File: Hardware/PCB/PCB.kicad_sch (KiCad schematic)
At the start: 74 parts, among them CN1 XT30UPB-M, CN2 2060-453-HDGC, CN3 2060-452-HDGC, CN4 2060-453-HDGC, CN6 2060-453-HDGC, CN7 2060-453-HDGC, J1 Connector, USB-TYPE-C-16P, SW1 TS-1187A-B-A-B, U1 RP2350B_C42415655, U3 BMP581, U4 ICM-45686, U5 BQ25883RGER, U6 LMR51430YFDDCR, U7 TPS630701RNMR, U8 GD25Q128ESIGR, X2 X322512MSB4SI

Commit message: finishing up schem
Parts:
- removed CN2, CN4, CN6, CN7: 2060-453-HDGC, easyeda2kicad:CONN-SMD_2060-453-HDGC, symbol easyeda2kicad:2060-453-HDGC
- removed CN3: 2060-452-HDGC, easyeda2kicad:CONN-SMD_2060-452-HDGC, symbol easyeda2kicad:2060-452-HDGC
- added U10, U11, U12, U9: KF128-2.54-3P, easyeda2kicad:CONN-TH_3P-P2.54_KF128-2.54-3P, symbol easyeda2kicad:KF128-2.54-3P
- added U2: KF128-2.54-2P, easyeda2kicad:CONN-TH_P2.54_KF128-2.54-2P, symbol easyeda2kicad:KF128-2.54-2P
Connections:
- net +7.5V: now also U9.2
- net GND: now also U10.3, U11.3, U12.3, U2.1, U9.3
- net at C2.1, CN1.2 (+), U5.13 (BAT)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: now also U2.2
- net at C23.2, C24.1, C26.2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: now also U10.2, U11.2, U12.2
- net at U1.23 (GPIO23): now also U12.1
- net at U1.22 (GPIO22): now also U10.1
- net at U1.21 (GPIO21): now also U9.1
- net at U1.25 (GPIO24): now also U11.1

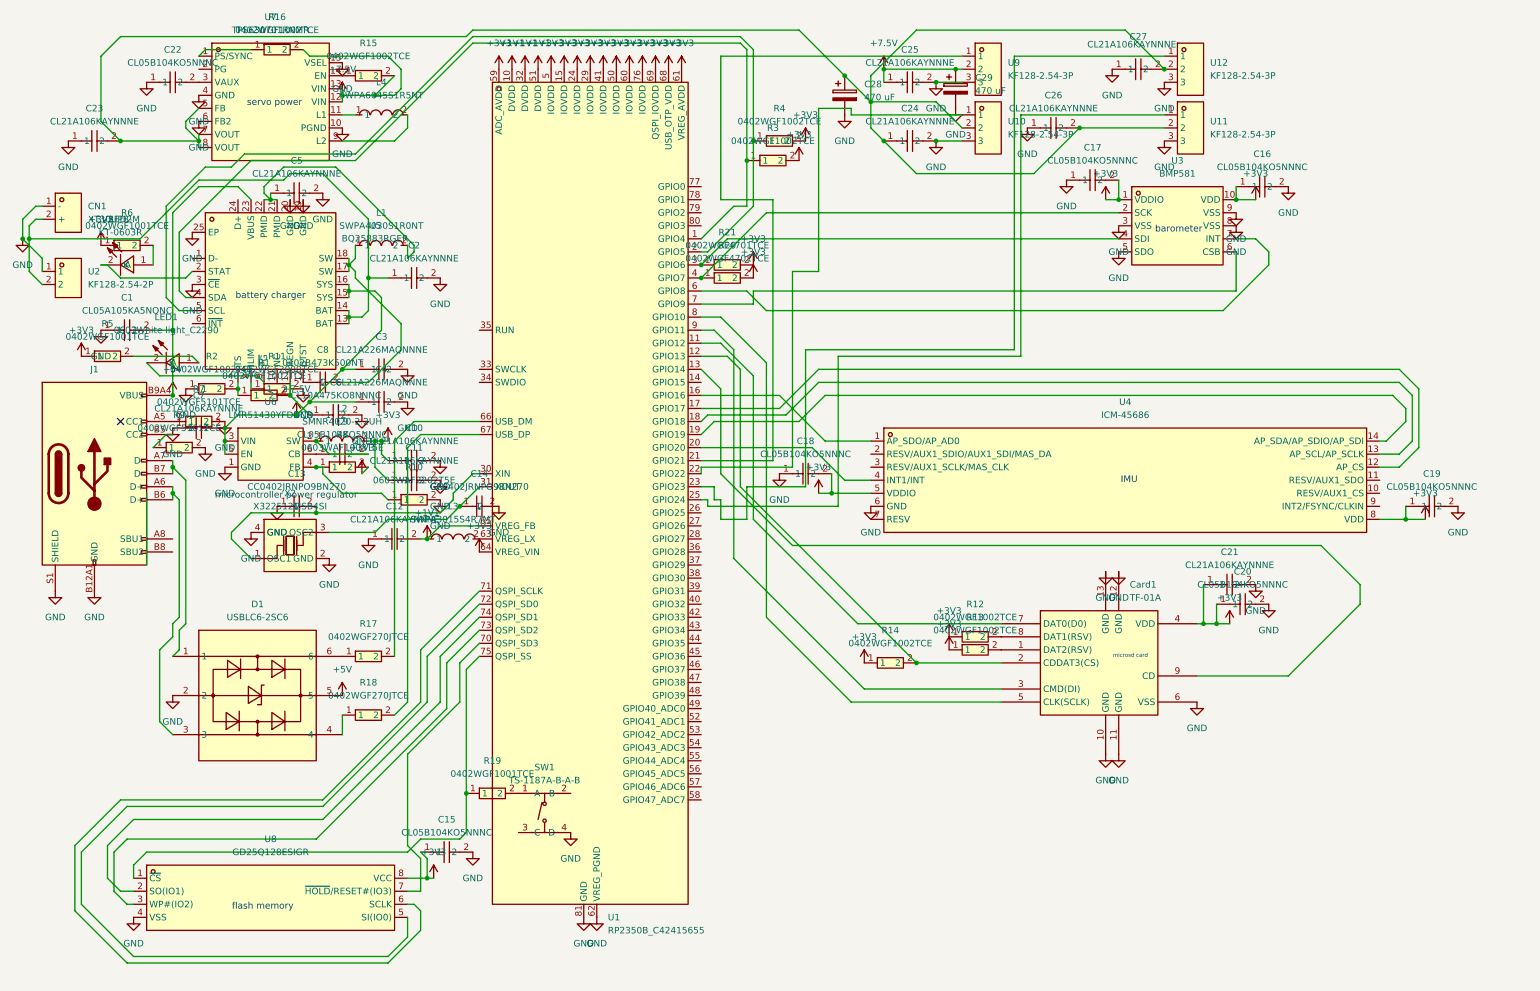
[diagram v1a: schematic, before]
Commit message: PCB routing started, added BOM.CSV
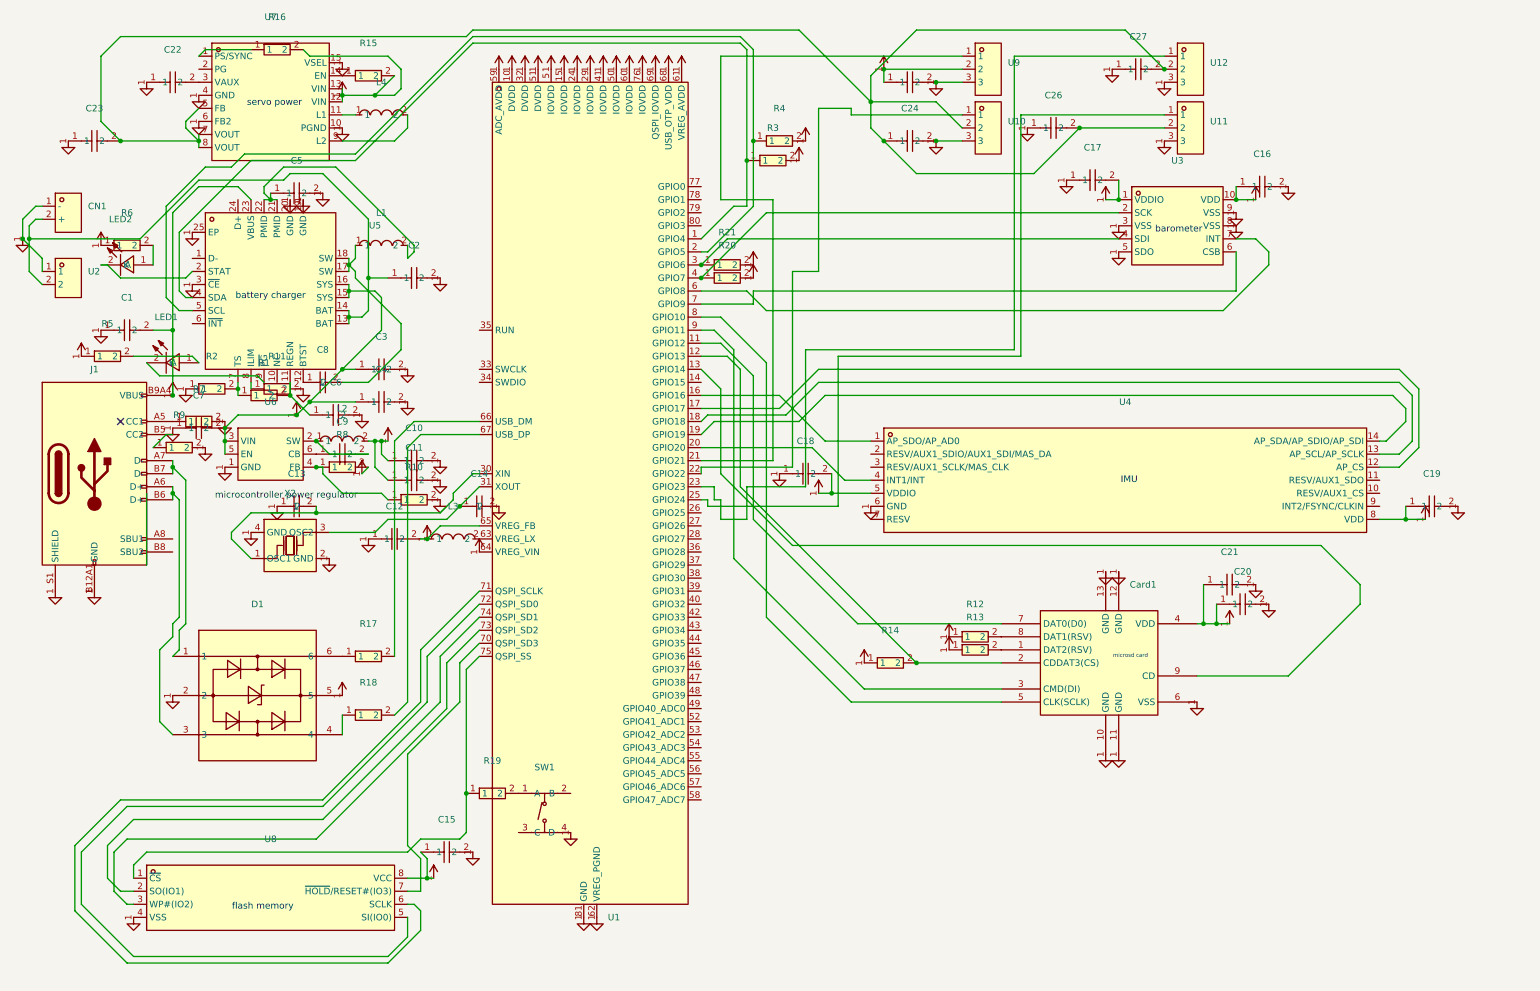
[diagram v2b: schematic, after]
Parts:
- removed C28, C29: 470 uF, Capacitor_SMD:CP_Elec_8x10.5, symbol Device:C_Polarized

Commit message: Battery charging added to PCB
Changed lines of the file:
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@@
 	)
 	(junction
+		(at 185.42 17.78)
+		(diameter 0)
+		(color 0 0 0 0)
+	)
+	(junction
 		(at 191.77 20.32)
 		(diameter 0)
@@
 		(at 33.02 86.36)
 	)
+	(bus_entry
+		(at 118.11 90.17)
+		(size 2.54 2.54)
+		(stroke
+			(width 0)
+			(type default)
+		)
+	)
 	(wire
 		(pts
@@
 	(wire
 		(pts
+			(xy 185.42 17.78) (xy 196.85 17.78)
+		)
+		(stroke
+			(width 0)
+			(type default)
+		)
+	)
+	(wire
+		(pts
 			(xy 71.12 90.17) (xy 73.66 92.71)
 		)
@@
 	(wire
 		(pts
-			(xy 181.61 17.78) (xy 196.85 17.78)
+			(xy 181.61 17.78) (xy 185.42 17.78)
 		)
 		(stroke
@@
 		)
 		(stroke
+			(width 0)
+			(type default)
+		)
+	)
+	(wire
+		(pts
+			(xy 185.42 19.05) (xy 185.42 17.78)
+		)
+		(stroke

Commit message: Restarting PCB, finished Flash memory application
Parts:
- added C28, C29, C30, C32, C33, C34, C35, C36, C37, C38, C39, C40: CL05B104KO5NNNC, easyeda2kicad:C0402, symbol easyeda2kicad:CL05B104KO5NNNC
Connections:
- net +1V1: now also C28.1, C29.1, C30.1
- net +3V3: now also C32.1, C33.1, C34.1, C35.1, C36.1, C37.1, C38.1, C39.1, C40.1
- net GND: now also C28.2, C29.2, C30.2, C32.2, C33.2, C34.2, C35.2, C36.2, C37.2, C38.2, C39.2, C40.2

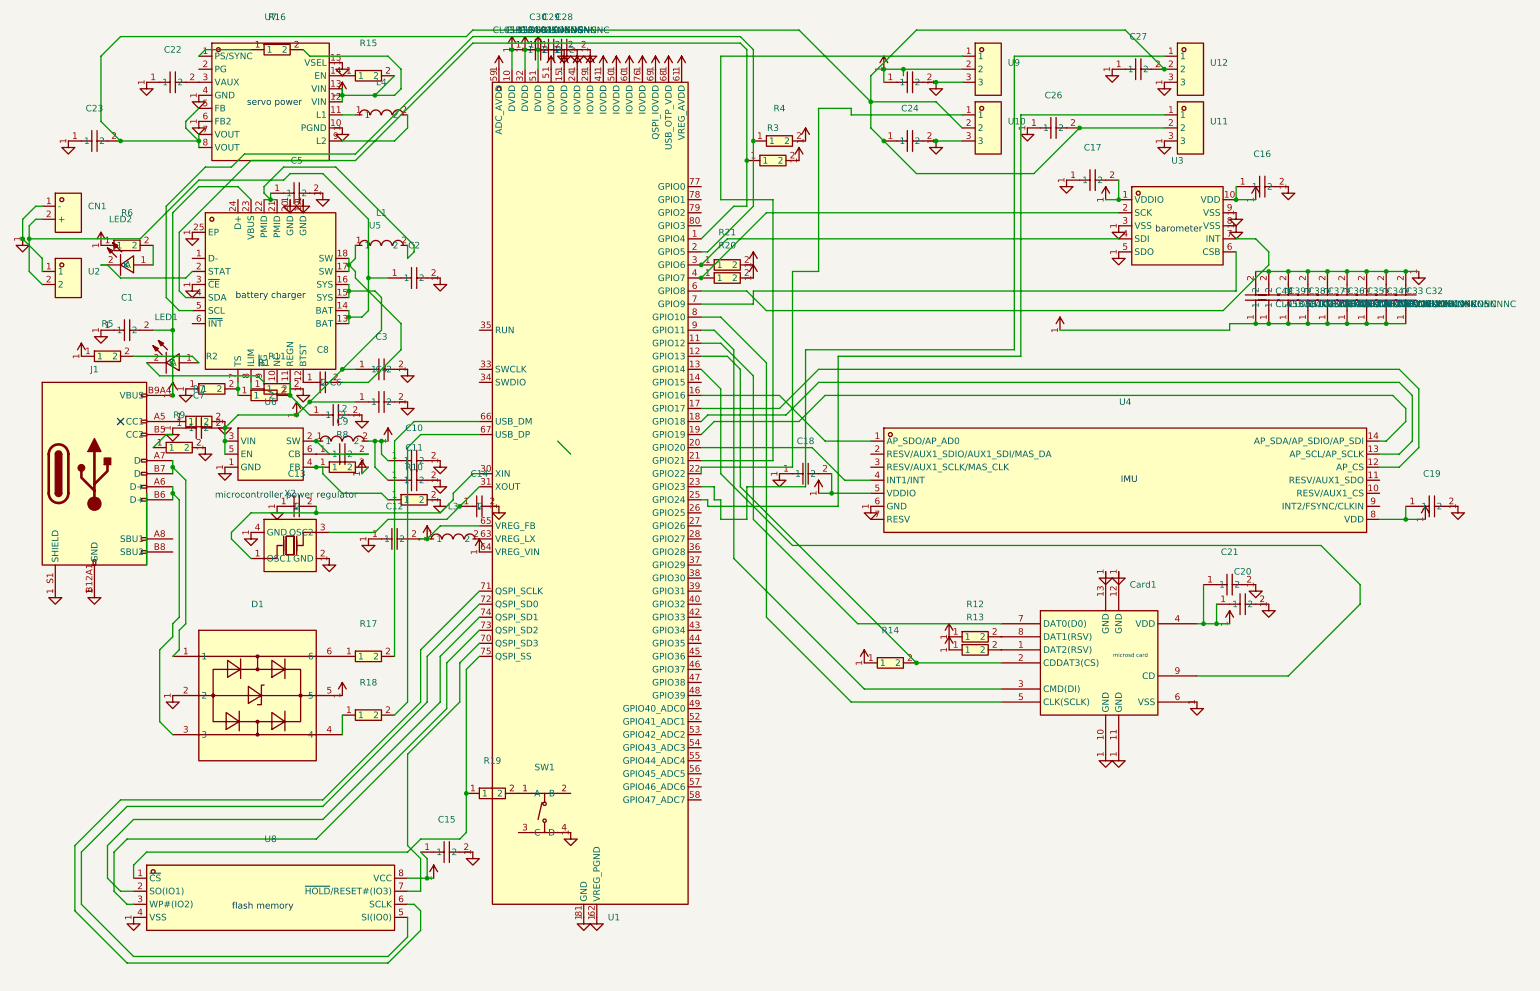
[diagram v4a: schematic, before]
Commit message: Got some advice, restarting entire project, applied integrated inductors to schematic, and restarted it
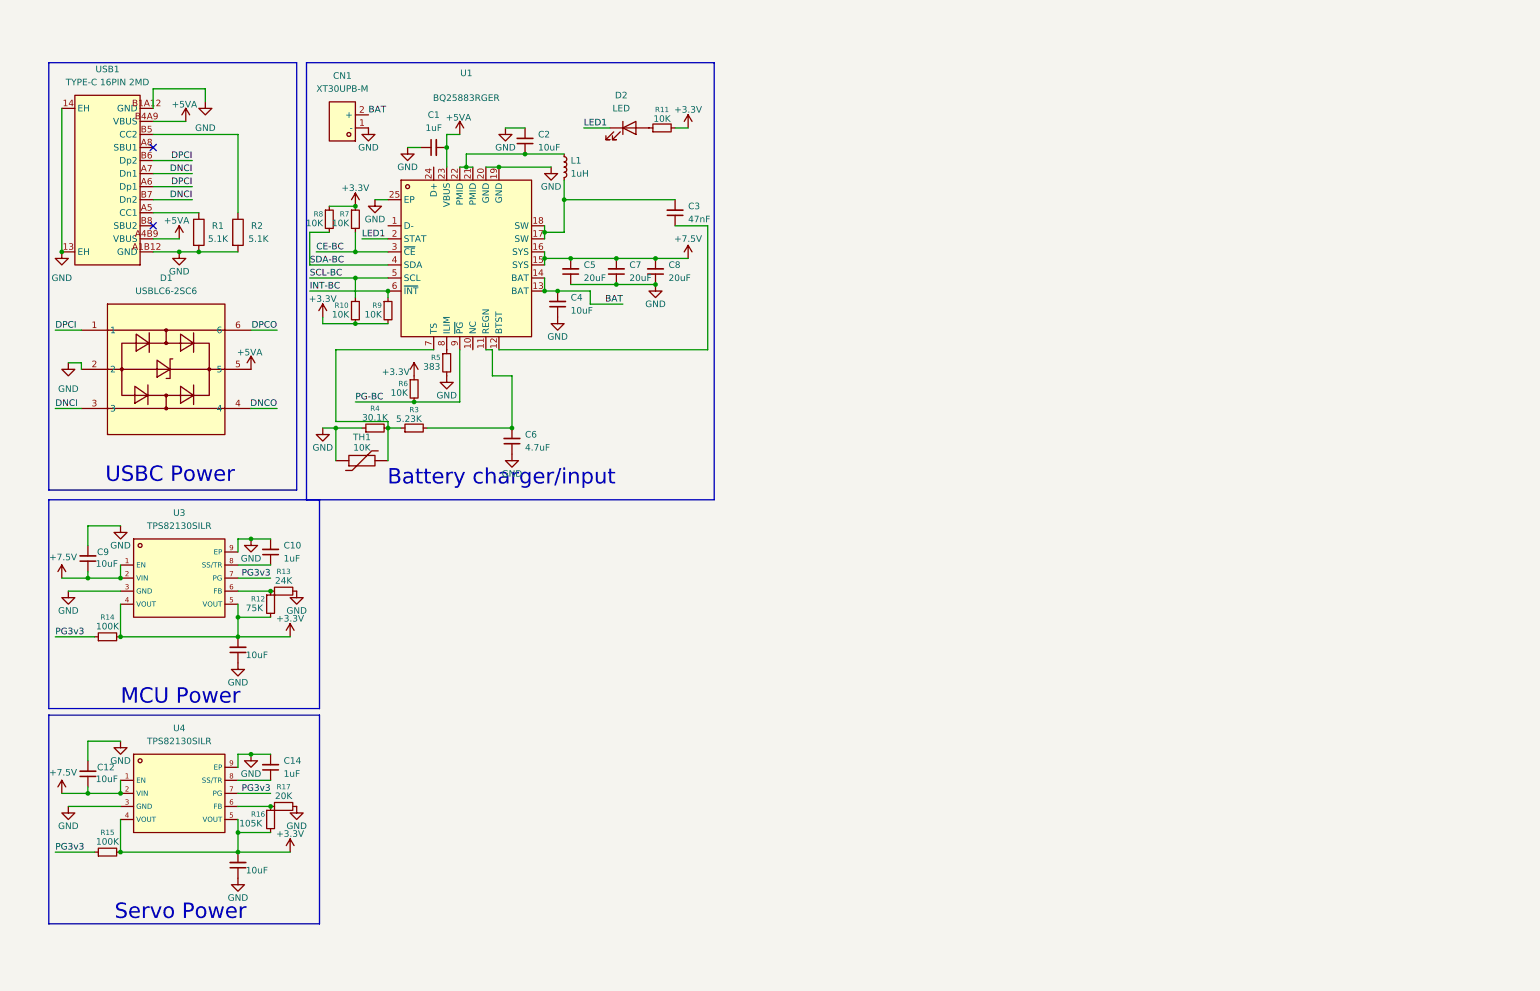
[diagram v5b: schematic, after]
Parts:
- removed C1: CL05A105KA5NQNC, easyeda2kicad:C0402, symbol easyeda2kicad:CL05A105KA5NQNC
- removed C10, C11, C12, C2, C21, C23, C24, C25, C26, C27, C5, C7: CL21A106KAYNNNE, easyeda2kicad:C0805, symbol easyeda2kicad:CL21A106KAYNNNE
- removed C13, C14: CC0402JRNPO9BN270, easyeda2kicad:C0402, symbol easyeda2kicad:CC0402JRNPO9BN270
- removed C15, C16, C17, C18, C19, C20, C22, C28, C29, C30, C32, C33, C34, C35, C36, C37, C38, C39, C40, C9: CL05B104KO5NNNC, easyeda2kicad:C0402, symbol easyeda2kicad:CL05B104KO5NNNC
- removed C3, C4: CL21A226MAQNNNE, easyeda2kicad:C0805, symbol easyeda2kicad:CL21A226MAQNNNE
- removed C6: CL10A475KO8NNNC, easyeda2kicad:C0603, symbol easyeda2kicad:CL10A475KO8NNNC
- removed C8: 0402B473K500NT, easyeda2kicad:C0402, symbol easyeda2kicad:0402B473K500NT
- removed CN1: XT30UPB-M, easyeda2kicad:CONN-TH_XT30UPB-M, symbol easyeda2kicad:XT30UPB-M
- removed Card1: TF-01A, easyeda2kicad:TF-SMD_TF-01A, symbol easyeda2kicad:TF-01A
- removed D1: USBLC6-2SC6, easyeda2kicad:SOT-23-6_L2.9-W1.6-P0.95-LS2.8-BL, symbol easyeda2kicad:USBLC6-2SC6
- removed J1: Connector, USB-TYPE-C-16P, PCM_JLCPCB:TYPE-C-SMD_HX-TYPE-C-16PIN, symbol PCM_JLCPCB-Extended:Connector, USB-TYPE-C-16P
- removed L1: SWPA4030S1R0NT, easyeda2kicad:IND-SMD_L4.0-W4.0_SWPA4018S, symbol easyeda2kicad:SWPA4030S1R0NT
- removed L2: SMNR4020-2.2UH, easyeda2kicad:IND-SMD_L4.0-W4.0_LQH44PN2R2MP0L, symbol easyeda2kicad:SMNR4020-2.2UH
- removed L3: SWPA3015S4R7MT, easyeda2kicad:IND-SMD_L3.0-W3.0_FNR30XXS, symbol easyeda2kicad:SWPA3015S4R7MT
- removed L4: SWPA6045S1R5NT, easyeda2kicad:IND-SMD_L6.0-W6.0_SWPA6045S, symbol easyeda2kicad:SWPA6045S1R5NT
- removed LED1: 0603White light_C2290, easyeda2kicad:LED0603-R-RD_WHITE, symbol easyeda2kicad:0603Whitelight_C2290
- removed LED2: KT-0603R, easyeda2kicad:LED-SMD_L1.6-W0.8-R-RD, symbol easyeda2kicad:KT-0603R
- removed R1, R12, R13, R14, R15, R16, R2, R3, R4: 0402WGF1002TCE, easyeda2kicad:R0402, symbol easyeda2kicad:0402WGF1002TCE
- removed R10: 0603WAF2202T5E, easyeda2kicad:R0603, symbol easyeda2kicad:0603WAF2202T5E
- removed R11: 0402WGF2000TCE, easyeda2kicad:R0402, symbol easyeda2kicad:0402WGF2000TCE
- removed R17, R18: 0402WGF270JTCE, easyeda2kicad:R0402, symbol easyeda2kicad:0402WGF270JTCE
- removed R19, R5, R6: 0402WGF1001TCE, easyeda2kicad:R0402, symbol easyeda2kicad:0402WGF1001TCE
- removed R20, R21: 0402WGF4701TCE, easyeda2kicad:R0402, symbol easyeda2kicad:0402WGF4701TCE
- removed R7, R9: 0402WGF5101TCE, easyeda2kicad:R0402, symbol easyeda2kicad:0402WGF5101TCE
- removed R8: 0603WAF1003T5E, easyeda2kicad:R0603, symbol easyeda2kicad:0603WAF1003T5E
- removed SW1: TS-1187A-B-A-B, easyeda2kicad:SW-SMD_4P-L5.1-W5.1-P3.70-LS6.5-TL_H1.5, symbol easyeda2kicad:TS-1187A-B-A-B
- removed U1: RP2350B_C42415655, easyeda2kicad:QFN-80_L10.0-W10.0-P0.40-TL-EP3.4, symbol easyeda2kicad:RP2350B_C42415655
- removed U10, U11, U12, U9: KF128-2.54-3P, easyeda2kicad:CONN-TH_3P-P2.54_KF128-2.54-3P, symbol easyeda2kicad:KF128-2.54-3P
- removed U2: KF128-2.54-2P, easyeda2kicad:CONN-TH_P2.54_KF128-2.54-2P, symbol easyeda2kicad:KF128-2.54-2P
- removed U3: BMP581, easyeda2kicad:LGA-10_L2.0-W2.0-P0.50-TL_BMP581, symbol easyeda2kicad:BMP581
- removed U4: ICM-45686, easyeda2kicad:LGA-14_L3.0-W2.5-P0.50-TL, symbol easyeda2kicad:ICM-45686
- removed U5: BQ25883RGER, easyeda2kicad:VFQFPN-24_L4.0-W4.0-P0.50-BL-EP2.8, symbol easyeda2kicad:BQ25883RGER
- removed U6: LMR51430YFDDCR, easyeda2kicad:SOT-23-6_L2.9-W1.6-P0.95-LS2.9-BL, symbol easyeda2kicad:LMR51430YFDDCR
- removed U7: TPS630701RNMR, easyeda2kicad:VQFN-HR-15_L3.0-W2.5-P0.50-BL_TPS63070RNMR, symbol easyeda2kicad:TPS630701RNMR
- removed U8: GD25Q128ESIGR, easyeda2kicad:SOP-8_L5.3-W5.3-P1.27-LS8.0-BL, symbol easyeda2kicad:GD25Q128ESIGR
- removed X2: X322512MSB4SI, easyeda2kicad:CRYSTAL-SMD_4P-L3.2-W2.5-BL, symbol easyeda2kicad:X322512MSB4SI
- added C1, C10, C14: 1uF, symbol Device:C_Small
- added C11, C12, C13, C2, C4, C9: 10uF, symbol Device:C_Small
- added C3: 47nF, symbol Device:C_Small
- added C5, C7, C8: 20uF, symbol Device:C_Small
- added C6: 4.7uF, symbol Device:C_Small
- added CN1: XT30UPB-M, easyeda2kicad:CONN-TH_XT30UPB-M, symbol OG FCFILE:XT30UPB-M
- added D1: USBLC6-2SC6, easyeda2kicad:SOT-23-6_L2.9-W1.6-P0.95-LS2.8-BL, symbol OG FCFILE:USBLC6-2SC6
- added D2: LED, symbol Device:LED
- added L1: 1uH, symbol Device:L_Small
- added R1, R2: 5.1K, symbol Device:R
- added R10, R11, R6, R7, R8, R9: 10K, symbol Device:R_Small
- added R12: 75K, symbol Device:R_Small
- added R13: 24K, symbol Device:R_Small
- added R14, R15: 100K, symbol Device:R_Small
- added R16: 105K, symbol Device:R_Small
- added R17: 20K, symbol Device:R_Small
- added R3: 5.23K, symbol Device:R_Small
- added R4: 30.1K, symbol Device:R_Small
- added R5: 383, symbol Device:R_Small
- added TH1: 10K, symbol Device:Thermistor
- added U1: BQ25883RGER, easyeda2kicad:VFQFPN-24_L4.0-W4.0-P0.50-BL-EP2.8, symbol OG FCFILE:BQ25883RGER
- added U3, U4: TPS82130SILR, lcsc_footprints:C473914_USIP-8_L3_0-W2_8-P0_65-TL-EP, symbol FCFILES:TPS82130SILR
- added USB1: TYPE-C 16PIN 2MD, easyeda2kicad:USB-C-SMD_TYPE-C-16PIN-2MD-073, symbol OG FCFILE:TYPE-C16PIN2MD
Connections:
- net +7.5V: now also C12.1, C5.2, C7.2, C8.2, C9.1, U1.15 (SYS), U1.16 (SYS), U3.1 (EN), U3.2 (VIN), U4.1 (EN), U4.2 (VIN)
- net GND: now also C1.1, C10.2, C11.1, C12.2, C13.1, C14.2, C2.2, C4.1, C5.1, C6.1, C7.1, C8.1, C9.2, CN1.1 (-), D1.2, R1.2, R13.2, R17.2, R2.2, R4.1, R5.2, TH1.1, U1.19 (GND), U1.20 (GND), U1.25 (EP), U3.3 (GND), U3.9 (EP), U4.3 (GND), U4.9 (EP), USB1.13 (EH), USB1.14 (EH), USB1.A1B12 (GND), USB1.B1A12 (GND)
- new net: R12.1, R13.1, U3.6 (FB)
- new net: C10.1, U3.8 (SS/TR)
- new net: C2.1, L1.1, U1.21 (PMID), U1.22 (PMID)
- new net: C3.2, L1.2, U1.17 (SW), U1.18 (SW)
- new net: R16.1, R17.1, U4.6 (FB)
- new net: C14.1, U4.8 (SS/TR)
- new net: R3.1, R4.2, TH1.2, U1.7 (TS)
- new net: R1.1, USB1.A5 (CC1)
- new net: R2.1, USB1.B5 (CC2)
- new net: D2.2 (A), R11.1
- new net: C6.2, R3.2, U1.11 (REGN)
- new net: C3.1, U1.12 (BTST)
- new net: R5.1, U1.8 (ILIM)
- new net +3.3V: C11.2, C13.2, R10.2, R11.2, R12.2, R14.2, R15.2, R16.2, R6.1, R7.1, R8.1, R9.2, U3.4 (VOUT), U3.5 (VOUT), U4.4 (VOUT), U4.5 (VOUT)
- new net +5VA: C1.2, D1.5, U1.23 (VBUS), USB1.A4B9 (VBUS), USB1.B4A9 (VBUS)
- new net BAT: C4.2, CN1.2 (+), U1.13 (BAT), U1.14 (BAT)
- new net CE-BC: R7.2, U1.3 (~{CE})
- new net DNCI: D1.3, USB1.A7 (Dn1), USB1.B7 (Dn2)
- new net DNCO: D1.4
- new net DPCI: D1.1, USB1.A6 (Dp1), USB1.B6 (Dp2)
- new net DPCO: D1.6
- new net INT-BC: R9.1, U1.6 (~{INT})
- new net LED1: D2.1 (K), U1.2 (STAT)
- new net PG-BC: R6.2, U1.9 (~{PG})
- new net PG3v3: R14.1, R15.1, U3.7 (PG), U4.7 (PG)
- new net SCL-BC: R10.1, U1.5 (SCL)
- new net SDA-BC: R8.2, U1.4 (SDA)
- no-connect marks 1 -> 2
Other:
- note added: "Battery charger/input"
- note added: "MCU Power"
- note added: "Servo Power"
- note added: "USBC Power"
- note removed: "IMU"
- note removed: "barometer"
- note removed: "battery charger"
- note removed: "flash memory"
- note removed: "microcontroller power regulator"
- note removed: "microsd card"
- note removed: "servo power"
